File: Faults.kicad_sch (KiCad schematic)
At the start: 20 parts, among them U4 LM393, U5 LM393, U8 LM393, U9 LM393

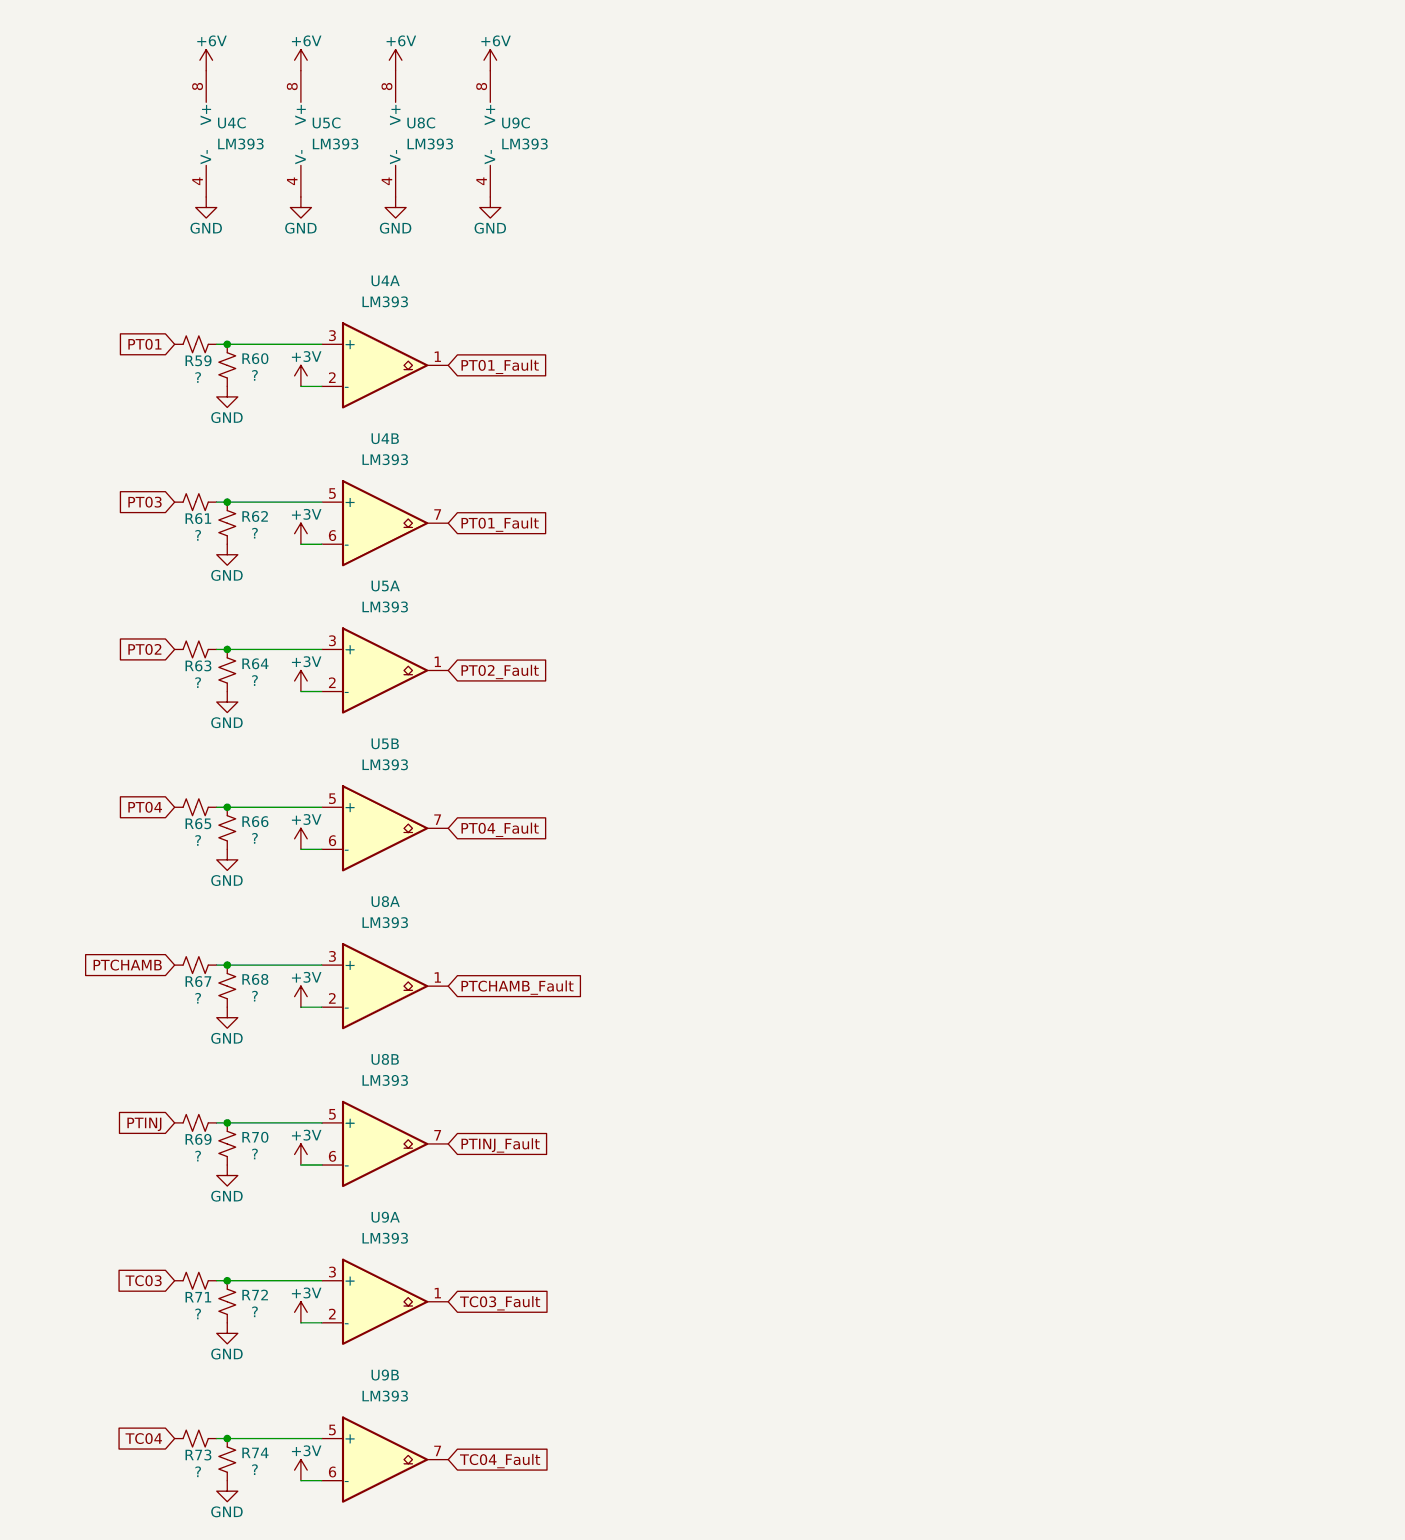
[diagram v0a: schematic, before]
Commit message: Purge Oscillator/Timer
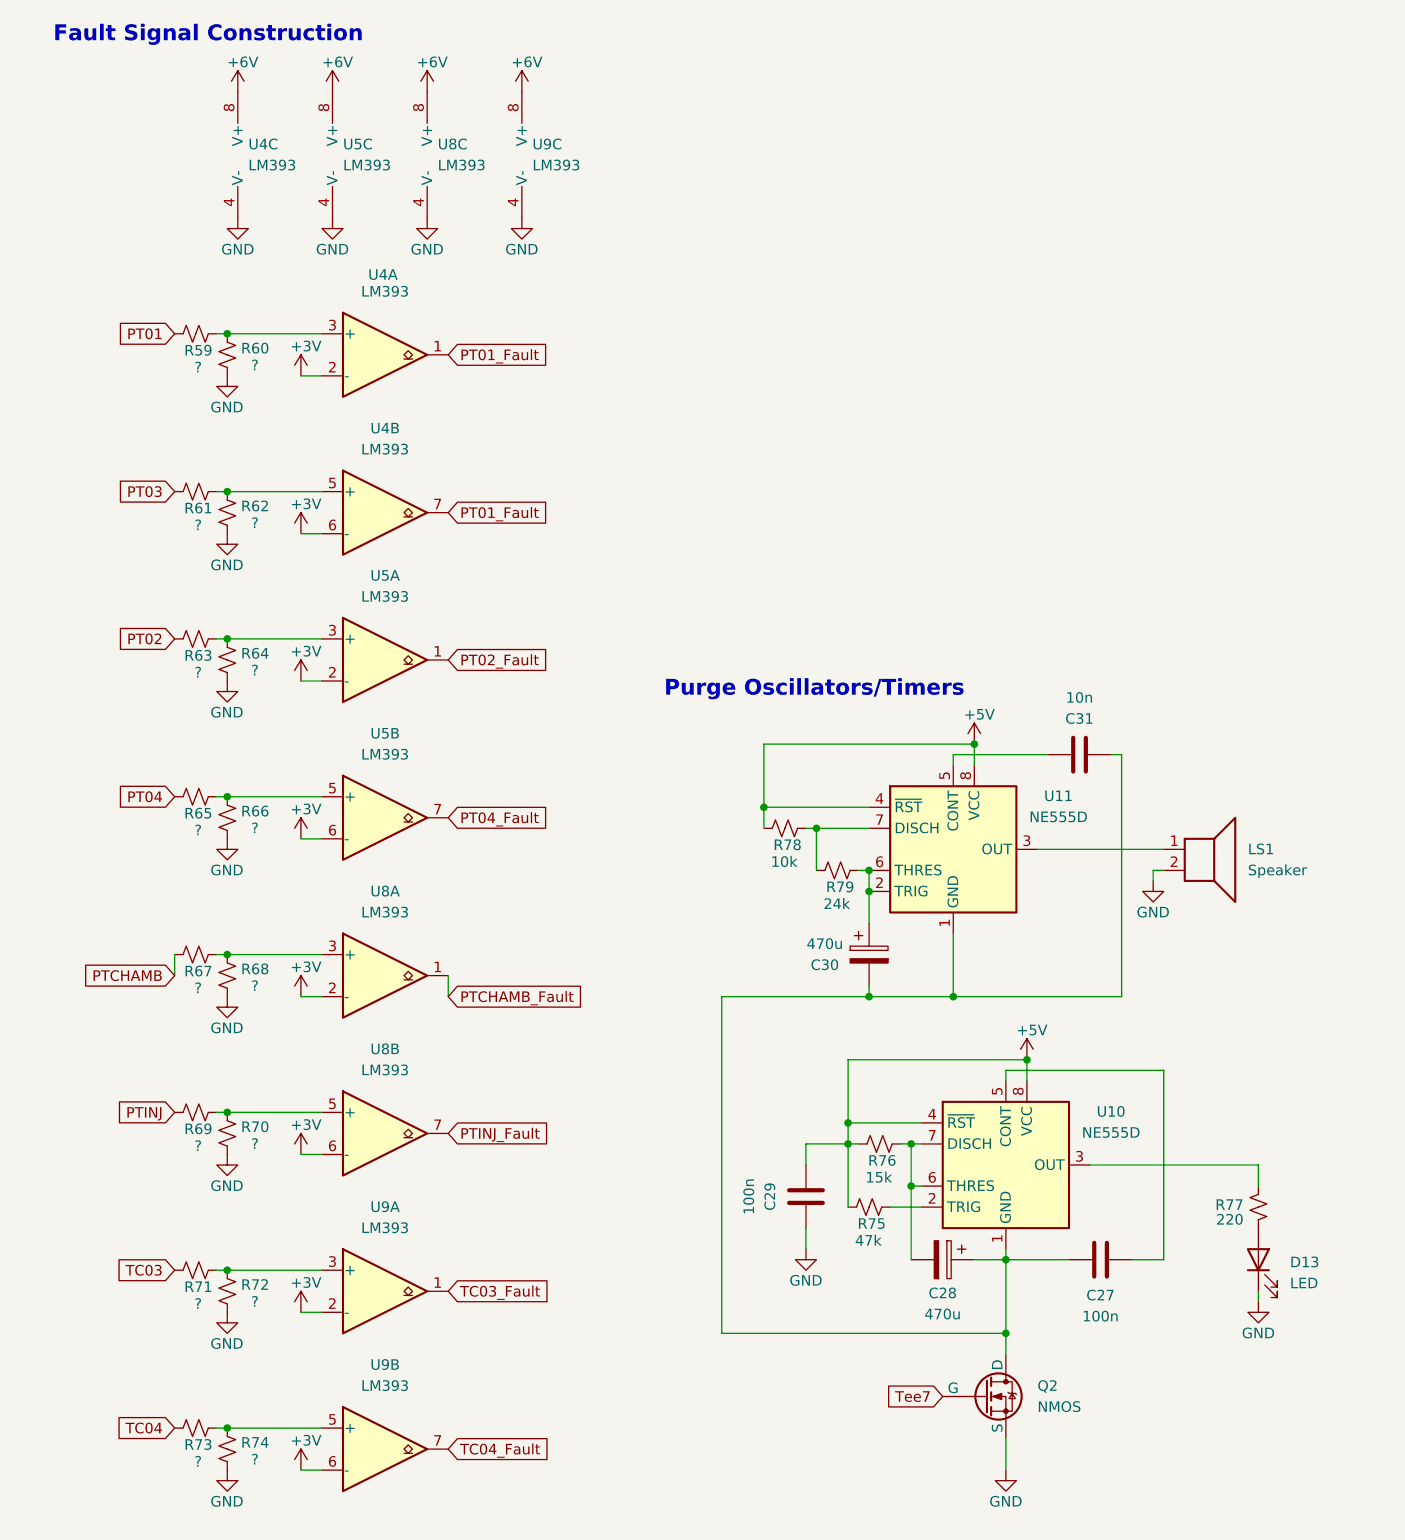
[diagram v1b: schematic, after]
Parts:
- added C27, C29: 100n, symbol Device:C
- added C28, C30: 470u, symbol Device:C_Polarized
- added C31: 10n, symbol Device:C
- added D13: LED, symbol Device:LED
- added LS1: Speaker, symbol Device:Speaker
- added Q2: NMOS, symbol Simulation_SPICE:NMOS
- added R75: 47k, symbol Device:R_Small_US
- added R76: 15k, symbol Device:R_Small_US
- added R77: 220, symbol Device:R_Small_US
- added R78: 10k, symbol Device:R_Small_US
- added R79: 24k, symbol Device:R_Small_US
- added U10, U11: NE555D, Package_SO:SOIC-8_3.9x4.9mm_P1.27mm, symbol Timer:NE555D
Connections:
- net GND: now also C29.2, D13.1 (K), LS1.2, Q2.3 (S)
- new net: C27.1, C28.1, C30.2, C31.2, Q2.1 (D), U10.1 (GND), U11.1 (GND)
- new net: LS1.1, U11.3 (OUT)
- new net: C31.1, U11.5 (CONT)
- new net: C27.2, U10.5 (CONT)
- new net: D13.2 (A), R77.2
- new net: C28.2, R76.2, U10.6 (THRES), U10.7 (DISCH)
- new net: C30.1, R79.2, U11.2 (TRIG), U11.6 (THRES)
- new net: R78.2, R79.1, U11.7 (DISCH)
- new net: R75.2, U10.2 (TRIG)
- new net: R77.1, U10.3 (OUT)
- new net +5V: C29.1, R75.1, R76.1, R78.1, U10.4 (~{RST}), U10.8 (VCC), U11.4 (~{RST}), U11.8 (VCC)
- new net Tee7: Q2.2 (G)
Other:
- note added: "Fault Signal Construction"
- note added: "Purge Oscillators/Timers"
- moved on the sheet: R59, R60, R61, R62, R63, R64, R65, R66, R67, R68, R69, R70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

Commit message: Voltage Fix, Tri-State Buffers, Double-Buffer
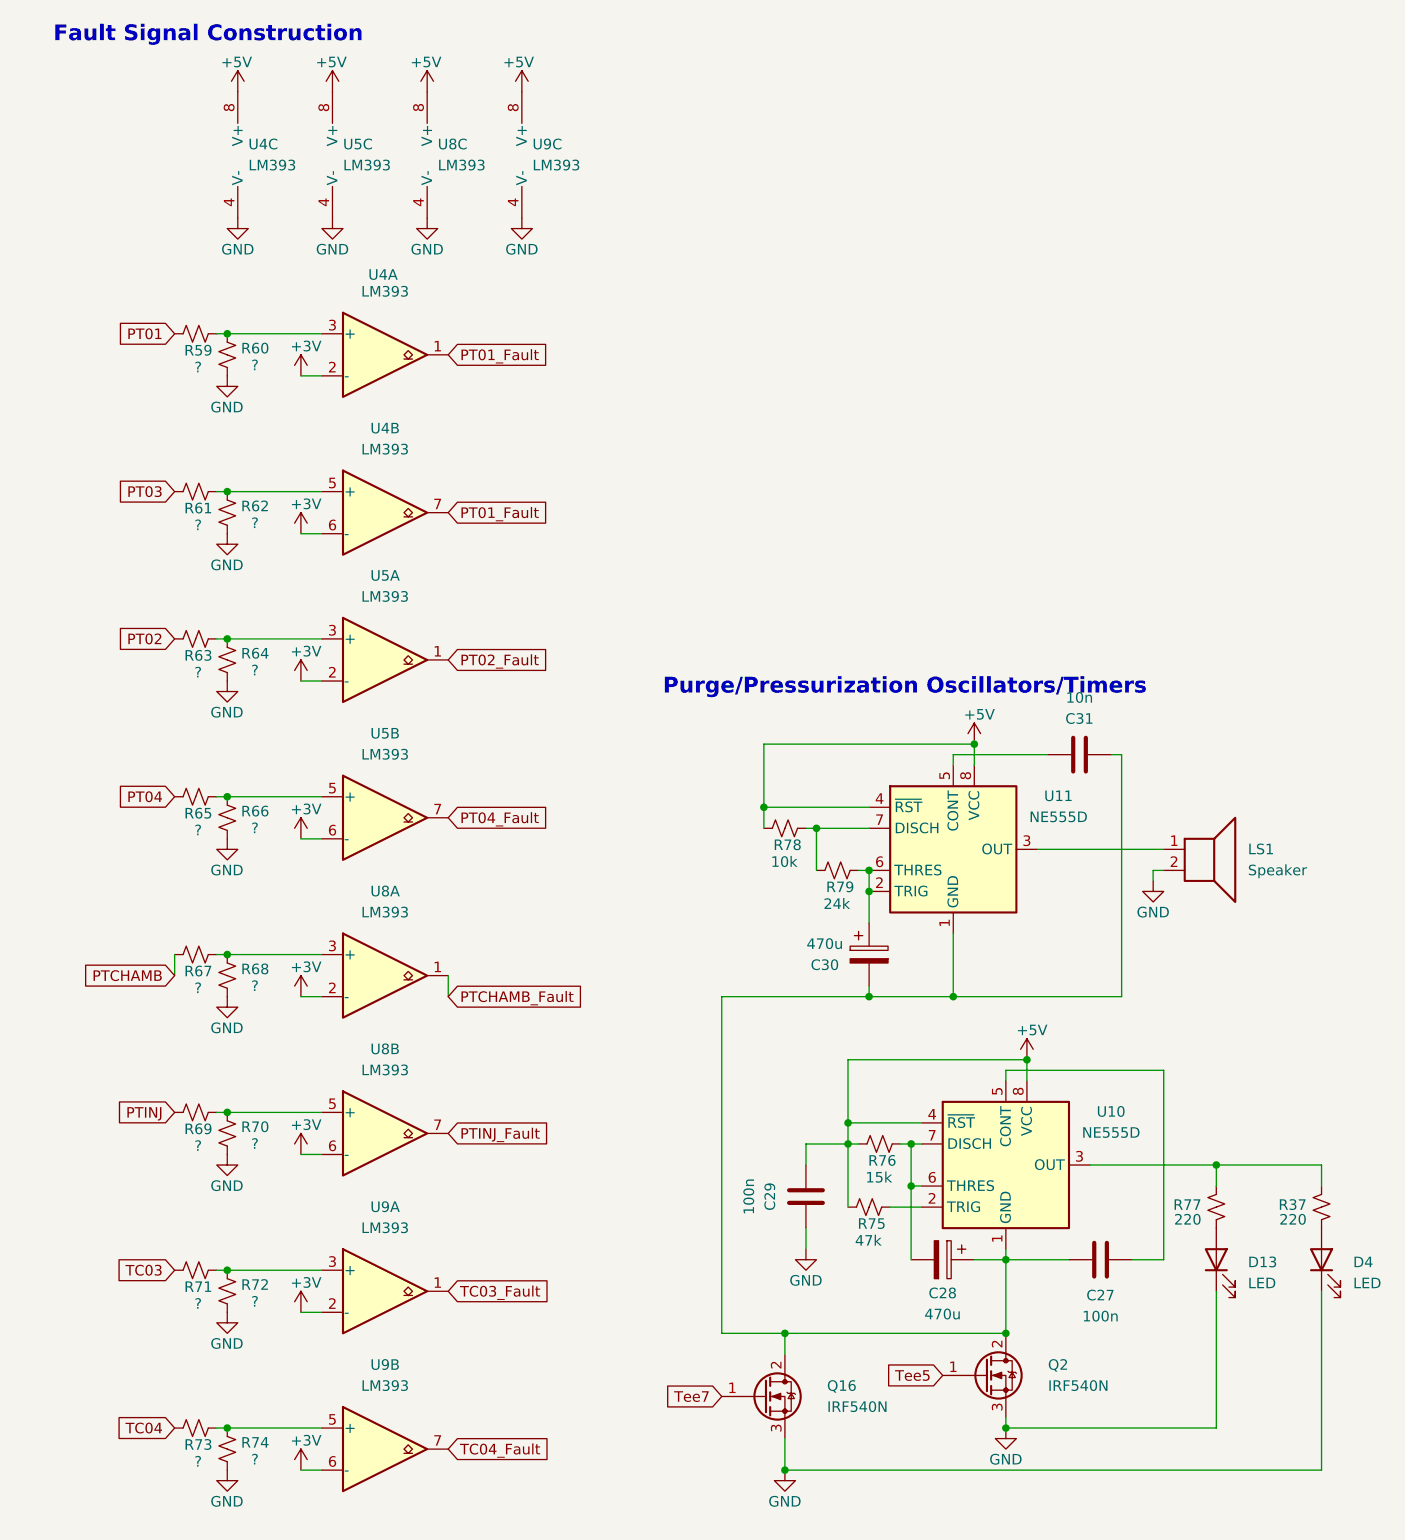
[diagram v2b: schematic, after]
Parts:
- removed Q2: NMOS, symbol Simulation_SPICE:NMOS
- added D4: LED, symbol Device:LED
- added Q16, Q2: IRF540N, Package_TO_SOT_THT:TO-220-3_Vertical, symbol Transistor_FET:IRF540N
- added R37: 220, symbol Device:R_Small_US
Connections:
- net +6V is gone; now on net +5V: U4.8 (V+), U5.8 (V+), U8.8 (V+), U9.8 (V+)
- net GND: now also D4.1 (K), Q16.3 (S), Q2.3 (S)
- net Tee7: now also Q16.1 (G)
- net at C27.1, C28.1, C30.2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: now also Q16.2 (D), Q2.2 (D)
- net at R77.1, U10.3 (OUT): now also R37.1
- new net: D4.2 (A), R37.2
- new net Tee5: Q2.1 (G)
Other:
- note added: "Purge/Pressurization Oscillators/Timers"
- note removed: "Purge Oscillators/Timers"
- moved on the sheet: D13, R77
